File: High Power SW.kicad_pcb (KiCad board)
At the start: 2 copper layers, 48 x 32 mm, 20 parts, among them CN1 Jumper_NC_Small, Q1 PSMN5R6-60YLX, U1 PS2801C-1-A

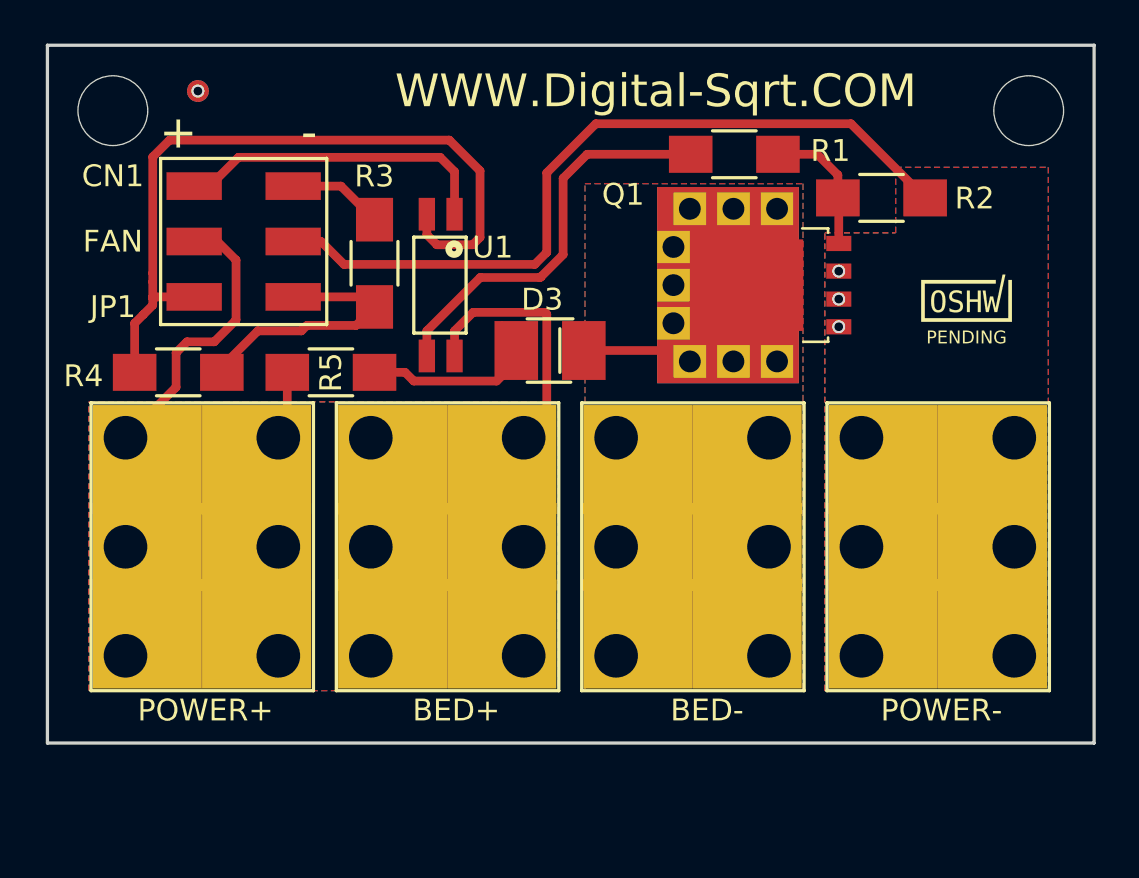
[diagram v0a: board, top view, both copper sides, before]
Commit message: Added OSHWA Number to board
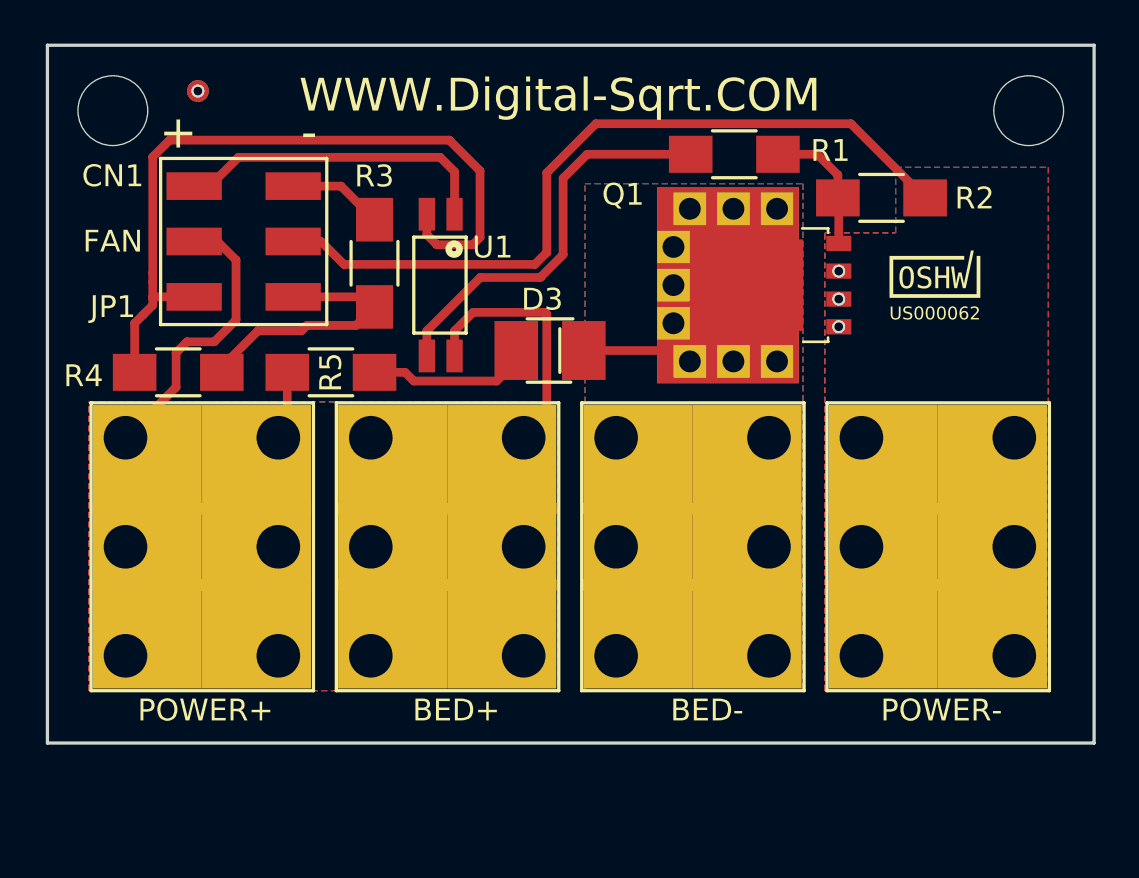
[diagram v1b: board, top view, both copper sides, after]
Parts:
- removed the REF*** at (108.5, 114.6)
- added REF***: OSHW-Symbol_6.7x6mm_SilkScreen, Symbols:OSHW-Symbol_6.7x6mm_SilkScreen, B.Cu at (107.8, 114.2)
- OSHW_Mono_0.1_Scale: value PENDING -> US000062
- moved OSHW_Mono_0.1_Scale 1.82 mm to (107.8, 113.4)
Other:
- board text added: "Little Driver"
- board text removed: "Small Driver"

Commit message: added more mounting holes
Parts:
- added ?: , Mounting_Holes:MountingHole_3.2mm_M3, F.Cu at (70.0, 136.0)
- added ?: , Mounting_Holes:MountingHole_3.2mm_M3, F.Cu at (112.0, 136.0)
- moved ? 0.14 mm to (112.0, 106.0)
- moved ? 0.14 mm to (70.0, 106.0)
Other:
- board size 48 x 32 mm -> 48 x 36 mm
- board text added: "Ver 1.8"
- board text removed: "Ver 1.7"
